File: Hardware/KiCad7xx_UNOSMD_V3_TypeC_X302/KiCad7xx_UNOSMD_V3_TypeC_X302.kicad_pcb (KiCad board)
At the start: 2 copper layers, 68.6 x 53.3 mm, 76 parts, among them J1 -, J2 PINHD-1X18, J3 USB_C_Receptacle_USB2.0JAE_DX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, T1 FDN340P, U1 MC33269ST, U2 LP2985-XXDBVR, U3 ATMEGA16U2, U4 ATMEGAXX8-MUR, U5 LMV358?MM, U6 BCM857BS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

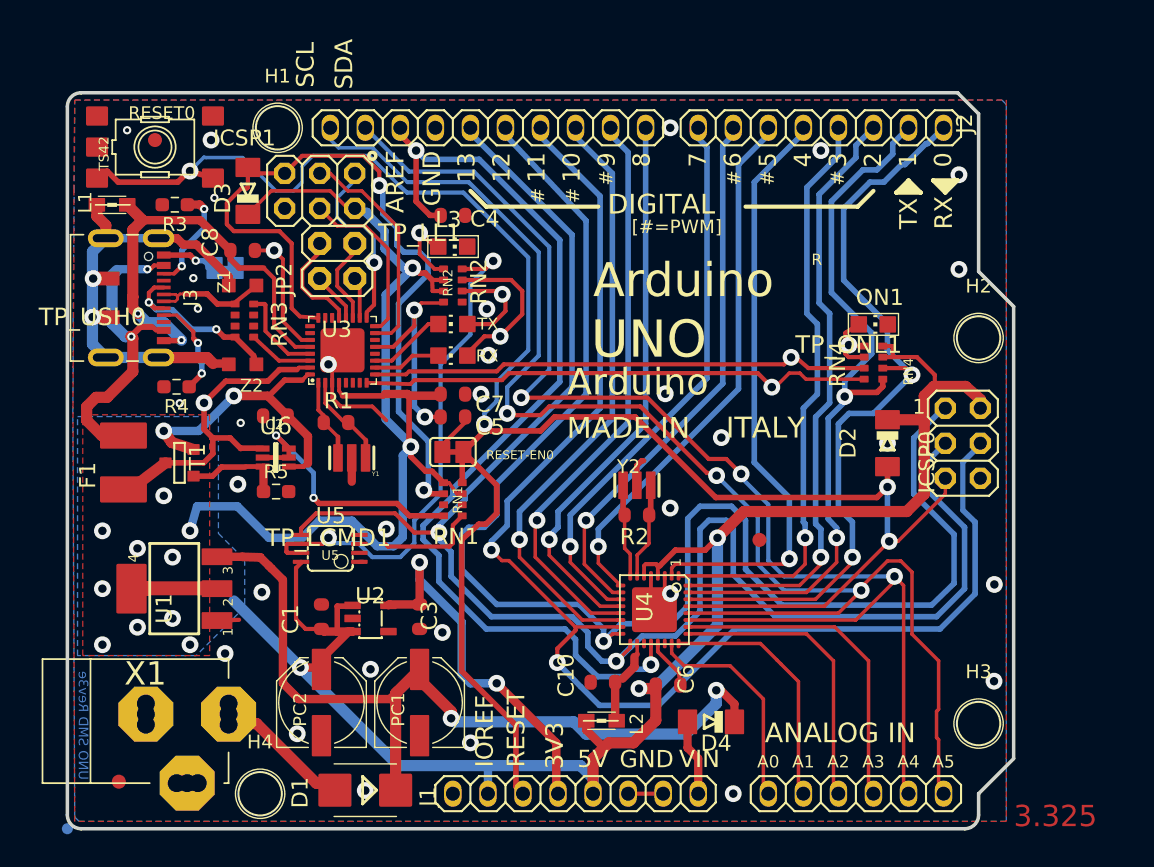
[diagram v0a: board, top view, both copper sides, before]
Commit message: Add:MURからAUパッケージへ基板データを変更
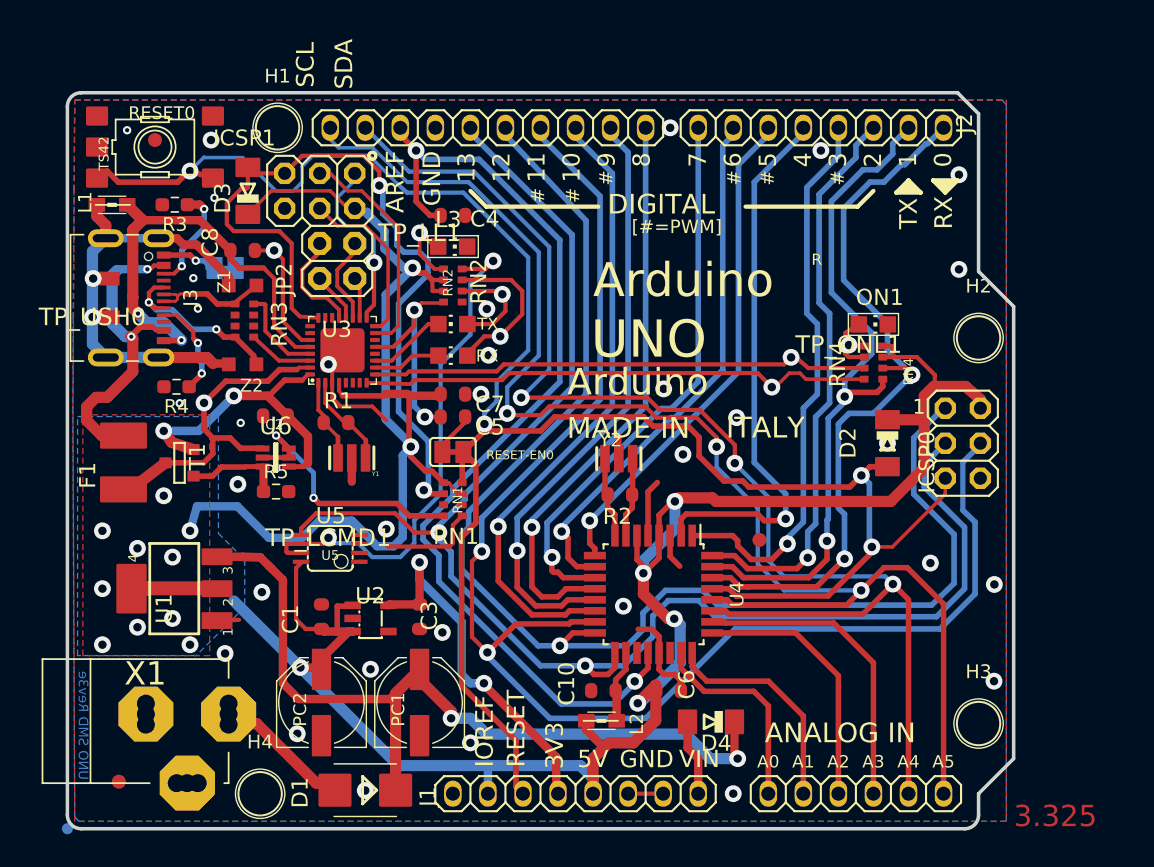
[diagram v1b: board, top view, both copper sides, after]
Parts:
- U4: footprint UNOSMD_V3:MLF32 -> Package_QFP:TQFP-32_7x7mm_P0.8mm
- moved Y2 2.33 mm to (154.2, 104.9)
- moved R2 1.92 mm to (154.3, 107.5)
- moved U4 1.12 mm to (156.7, 114.7)
- moved C10 0.61 mm to (153.1, 121.7)
- moved C6 0.41 mm to (157.8, 121.7)
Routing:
- net /MISO: track 107.1 -> 97.5 mm
- net /MOSI: track 97.4 -> 106.1 mm
- net /SCK: track 119.6 -> 111.8 mm
- net +5V: track 237.1 -> 244.0 mm, vias 17 -> 19
- net GND: track 33.3 -> 38.5 mm, vias 32 -> 33
- net /IO4: track 43.1 -> 39.9 mm
- net /IO2: track 44.4 -> 41.4 mm
- net /IO1: track 52.4 -> 49.6 mm
- net /IO0: track 56.4 -> 53.6 mm
- net /IO5: track 38.9 -> 36.5 mm
- net /RESET: track 154.3 -> 151.9 mm
- net /IO3: track 42.9 -> 40.6 mm
- net /SS: track 44.4 -> 46.0 mm
- net /A2: track 21.1 -> 19.6 mm
- net /IO9: track 42.5 -> 44.0 mm
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
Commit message: Add:基板レイアウトを微修正
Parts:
- removed TP_LL1: TP_SP, UNOSMD_V3:TP-SP
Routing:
- net GND: track 38.5 -> 56.0 mm, vias 33 -> 35
- net Net-(TP_LL1-TESTP): track 5.46 -> 1.78 mm, vias 1 -> 0
- net /SCK: track 111.8 -> 110.7 mm
- net /RESET: track 151.9 -> 152.9 mm
- net /A2: track 19.6 -> 20.5 mm
- net /A3: track 23.0 -> 23.8 mm
- net /MOSI: track 106.1 -> 105.4 mm
- net /IO0: track 53.6 -> 54.2 mm

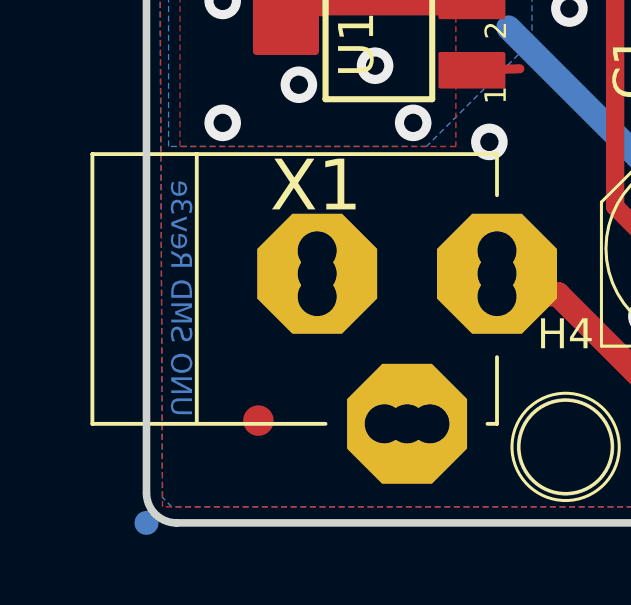
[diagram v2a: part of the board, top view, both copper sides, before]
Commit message: Add:基板デザインに'UNO-C X302'文字の追加
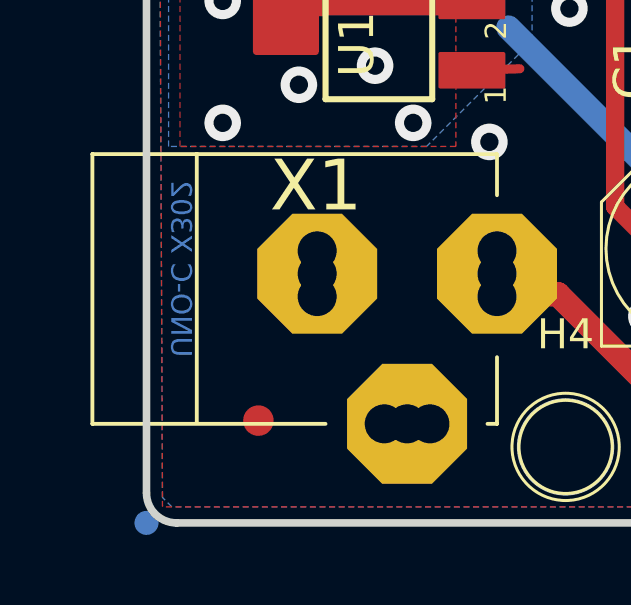
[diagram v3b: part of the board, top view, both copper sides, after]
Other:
- board text added: "UNO-C X302"
- board text removed: "UNO SMD Rev3e"
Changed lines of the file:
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@@
     (effects (font (size 1.542288 1.542288) (thickness 0.134112)) (justify left bottom))
   )
-  (gr_text "UNO SMD Rev3e" (at 115.7605 120.2436 -90) (layer "B.Cu")
+  (gr_text "UNO-C X302" (at 115.7605 120.2436 270) (layer "B.Cu")
     (effects (font (size 0.69088 0.69088) (thickness 0.12192)) (justify right top mirror))
   )
